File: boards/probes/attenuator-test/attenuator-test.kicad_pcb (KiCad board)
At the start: 4 copper layers, 45.6 x 10 mm, 7 parts, among them J1 Conn_Coaxial, J2 Conn_Coaxial

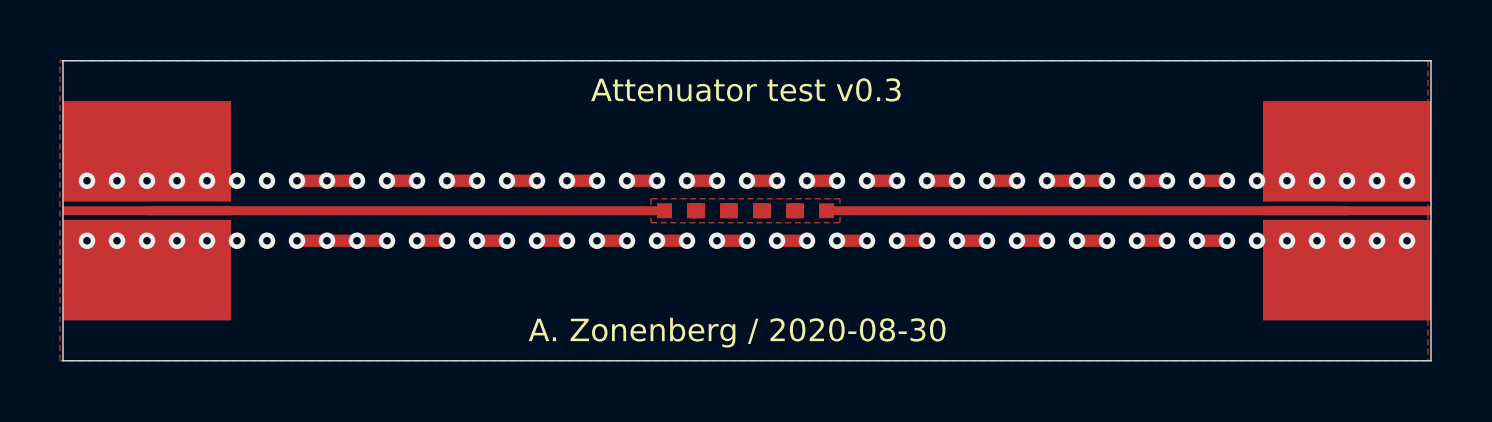
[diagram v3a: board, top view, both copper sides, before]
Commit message: Updated attenuator test with 4 overlapping resistor footprints
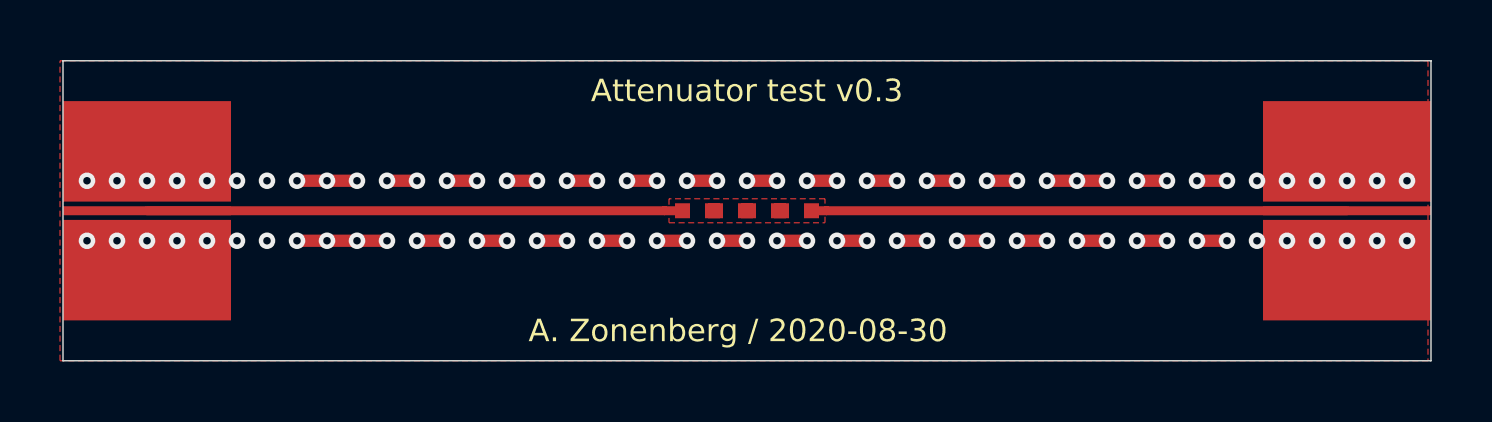
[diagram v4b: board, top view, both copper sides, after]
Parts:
- removed R2: 50, azonenberg_pcb:EIA_0402_RES_NOSILK_FLIPCHIP
- R3: value 100 -> 50
- R6: value 100 -> 200
- moved R3 0.50 mm to (128.3, 80.0)
- moved R4 0.50 mm to (129.4, 80.0)
- moved R5 0.50 mm to (130.6, 80.0)
- moved R6 0.50 mm to (131.7, 80.0)
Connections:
- R3 pad 2: Net-(R2-Pad1) -> /SIGNAL
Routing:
- net /SIGNAL: track 17.2 -> 17.8 mm
- net Net-(J2-Pad1): track 17.3 -> 17.8 mm
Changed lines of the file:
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@@
     (thickness 1.6)
     (drawings 6)
-    (tracks 184)
+    (tracks 186)
     (zones 0)
-    (modules 7)
-    (nets 8)
+    (modules 6)
+    (nets 7)
   )
   (page A4)
@@
   (net 2 /SIGNAL)
   (net 3 "Net-(J2-Pad1)")
-  (net 4 "Net-(R2-Pad1)")
-  (net 5 "Net-(R3-Pad1)")
-  (net 6 "Net-(R4-Pad1)")
-  (net 7 "Net-(R5-Pad1)")
+  (net 4 "Net-(R3-Pad1)")
+  (net 5 "Net-(R4-Pad1)")
+  (net 6 "Net-(R5-Pad1)")
   (net_class Default "This is the default net class."
     (clearance 0.15)
@@
     (add_net /SIGNAL)
     (add_net "Net-(J2-Pad1)")
-    (add_net "Net-(R2-Pad1)")
     (add_net "Net-(R3-Pad1)")
     (add_net "Net-(R4-Pad1)")
@@
   )
   (module azonenberg_pcb:EIA_0402_RES_NOSILK_FLIPCHIP (layer F.Cu)
-    (at 132.15 80 180)
+    (at 131.65 80 180)
     (solder_paste_margin -0.06)
     (fp_text reference R6 (at 0 1.5) (layer F.SilkS) hide
       (effects (font (size 1 1) (thickness 0.15)))
     )
-    (fp_text value 100 (at 0 3.5) (layer F.SilkS) hide
+    (fp_text value 200 (at 0 3.5) (layer F.SilkS) hide
       (effects (font (size 1 1) (thickness 0.15)))
     )
     (pad 2 smd rect (at 0.5 0 180) (size 0.5 0.5) (layers F.Cu F.Paste F.Mask)
-      (net 7 "Net-(R5-Pad1)"))
+      (net 6 "Net-(R5-Pad1)"))
     (pad 1 smd rect (at -0.5 0 180) (size 0.5 0.5) (layers F.Cu F.Paste F.Mask)
       (net 3 "Net-(J2-Pad1)"))
@@
   )
   (module azonenberg_pcb:EIA_0402_RES_NOSILK_FLIPCHIP (layer F.Cu)
-    (at 131.05 80 180)
+    (at 130.55 80 180)
     (solder_paste_margin -0.06)
     (fp_text reference R5 (at 0 1.5) (layer F.SilkS) hide
@@
     )
     (pad 2 smd rect (at 0.5 0 180) (size 0.5 0.5) (layers F.Cu F.Paste F.Mask)
-      (net 6 "Net-(R4-Pad1)"))
+      (net 5 "Net-(R4-Pad1)"))
     (pad 1 smd rect (at -0.5 0 180) (size 0.5 0.5) (layers F.Cu F.Paste F.Mask)
-      (net 7 "Net-(R5-Pad1)"))
+      (net 6 "Net-(R5-Pad1)"))
     (model /nfs4/home/azonenberg/kicad-libs/3rdparty/walter/smd_resistors/r_0402.wrl
       (at (xyz 0 0 0))
@@
   )
   (module azonenberg_pcb:EIA_0402_RES_NOSILK_FLIPCHIP (layer F.Cu)
-    (at 129.95 80 180)
+    (at 129.45 80 180)
     (solder_paste_margin -0.06)
     (fp_text reference R4 (at 0 1.5) (layer F.SilkS) hide
@@
     )
     (pad 2 smd rect (at 0.5 0 180) (size 0.5 0.5) (layers F.Cu F.Paste F.Mask)
-      (net 5 "Net-(R3-Pad1)"))
+      (net 4 "Net-(R3-Pad1)"))
     (pad 1 smd rect (at -0.5 0 180) (size 0.5 0.5) (layers F.Cu F.Paste F.Mask)
-      (net 6 "Net-(R4-Pad1)"))
+      (net 5 "Net-(R4-Pad1)"))
     (model /nfs4/home/azonenberg/kicad-libs/3rdparty/walter/smd_resistors/r_0402.wrl
       (at (xyz 0 0 0))
@@
   )
   (module azonenberg_pcb:EIA_0402_RES_NOSILK_FLIPCHIP (layer F.Cu)
-    (at 128.85 80 180)
+    (at 128.35 80 180)
     (solder_paste_margin -0.06)
     (fp_text reference R3 (at 0 1.5) (layer F.SilkS) hide
-      (effects (font (size 1 1) (thickness 0.15)))
-    )
-    (fp_text value 100 (at 0 3.5) (layer F.SilkS) hide
-      (effects (font (size 1 1) (thickness 0.15)))
-    )
-    (pad 2 smd rect (at 0.5 0 180) (size 0.5 0.5) (layers F.Cu F.Paste F.Mask)
-      (net 4 "Net-(R2-Pad1)"))
-    (pad 1 smd rect (at -0.5 0 180) (size 0.5 0.5) (layers F.Cu F.Paste F.Mask)
-      (net 5 "Net-(R3-Pad1)"))
-    (model /nfs4/home/azonenberg/kicad-libs/3rdparty/walter/smd_resistors/r_0402.wrl
-      (at (xyz 0 0 0))
-      (scale (xyz 1 1 1))
-      (rotate (xyz 0 0 0))
-    )
-  )
-  (module azonenberg_pcb:EIA_0402_RES_NOSILK_FLIPCHIP (layer F.Cu)
-    (at 127.75 80 180)
-    (solder_paste_margin -0.06)
-    (fp_text reference R2 (at 0 1.5) (layer F.SilkS) hide
       (effects (font (size 1 1) (thickness 0.15)))
     )
@@
       (net 2 /SIGNAL))
     (pad 1 smd rect (at -0.5 0 180) (size 0.5 0.5) (layers F.Cu F.Paste F.Mask)
-      (net 4 "Net-(R2-Pad1)"))
+      (net 4 "Net-(R3-Pad1)"))
     (model /nfs4/home/azonenberg/kicad-libs/3rdparty/walter/smd_resistors/r_0402.wrl
       (at (xyz 0 0 0))
@@
   (segment (start 151 81) (end 152 81) (width 0.3) (layer F.Cu) (net 1) (status 30))
   (segment (start 127.25 80) (end 110 80) (width 0.3) (layer F.Cu) (net 2) (status 30))
+  (segment (start 127.25 80) (end 127.85 80) (width 0.3) (layer F.Cu) (net 2))
   (segment (start 132.65 80) (end 150 80) (width 0.3) (layer F.Cu) (net 3) (status 30))
+  (segment (start 132.65 80) (end 132.15 80) (width 0.3) (layer F.Cu) (net 3))
   (zone (net 1) (net_name /GND) (layer In1.Cu) (hatch edge 0.508)
     (connect_pads yes (clearance 0.2))
@@
     (polygon
       (pts
-        (xy 126.8 79.6) (xy 126.8 80.4) (xy 133.1 80.4) (xy 133.1 79.6)
+        (xy 127.4 79.6) (xy 127.4 80.4) (xy 132.6 80.4) (xy 132.6 79.6)
       )
     )
@@
     (polygon
       (pts
-        (xy 126.5 79.5) (xy 126.5 80.5) (xy 126.7 80.5) (xy 126.7 79.5)
-      )
-    )
-    (polygon
-      (pts
-        (xy 133.2 79.5) (xy 133.2 80.5) (xy 133.4 80.5) (xy 133.4 79.5)
-      )
-    )
+        (xy 127.1 79.5) (xy 127.1 80.5) (xy 127.3 80.5) (xy 127.3 79.5)
+      )
+    )
+    (polygon
+      (pts
+        (xy 132.7 79.5) (xy 132.7 80.5) (xy 132.9 80.5) (xy 132.9 79.5)
+      )
+    )

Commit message: Attenuator test with 3 resistors
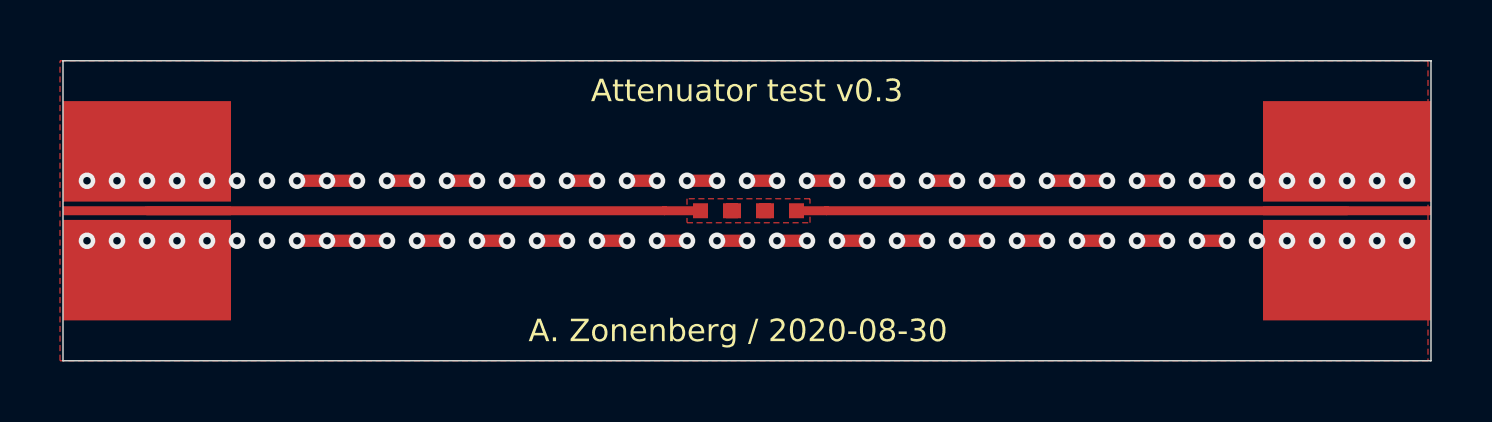
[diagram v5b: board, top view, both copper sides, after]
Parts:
- removed R3: 50, azonenberg_pcb:EIA_0402_RES_NOSILK_FLIPCHIP
- R4: value 100 -> 50
- R5: value 100 -> 200
- moved R4 0.50 mm to (128.9, 80.0)
- moved R5 0.50 mm to (130.1, 80.0)
- moved R6 0.50 mm to (131.2, 80.0)
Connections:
- R4 pad 2: Net-(R3-Pad1) -> /SIGNAL
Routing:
- net /SIGNAL: track 17.8 -> 18.4 mm
- net Net-(J2-Pad1): track 17.8 -> 18.3 mm
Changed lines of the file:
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@@
     (tracks 186)
     (zones 0)
-    (modules 6)
-    (nets 7)
+    (modules 5)
+    (nets 6)
   )
   (page A4)
@@
   (net 2 /SIGNAL)
   (net 3 "Net-(J2-Pad1)")
-  (net 4 "Net-(R3-Pad1)")
-  (net 5 "Net-(R4-Pad1)")
-  (net 6 "Net-(R5-Pad1)")
+  (net 4 "Net-(R4-Pad1)")
+  (net 5 "Net-(R5-Pad1)")
   (net_class Default "This is the default net class."
     (clearance 0.15)
@@
     (add_net /SIGNAL)
     (add_net "Net-(J2-Pad1)")
-    (add_net "Net-(R3-Pad1)")
     (add_net "Net-(R4-Pad1)")
     (add_net "Net-(R5-Pad1)")
   )
   (module azonenberg_pcb:EIA_0402_RES_NOSILK_FLIPCHIP (layer F.Cu)
-    (at 131.65 80 180)
+    (at 131.15 80 180)
     (solder_paste_margin -0.06)
     (fp_text reference R6 (at 0 1.5) (layer F.SilkS) hide
@@
     )
     (pad 2 smd rect (at 0.5 0 180) (size 0.5 0.5) (layers F.Cu F.Paste F.Mask)
-      (net 6 "Net-(R5-Pad1)"))
+      (net 5 "Net-(R5-Pad1)"))
     (pad 1 smd rect (at -0.5 0 180) (size 0.5 0.5) (layers F.Cu F.Paste F.Mask)
       (net 3 "Net-(J2-Pad1)"))
@@
   )
   (module azonenberg_pcb:EIA_0402_RES_NOSILK_FLIPCHIP (layer F.Cu)
-    (at 130.55 80 180)
+    (at 130.05 80 180)
     (solder_paste_margin -0.06)
     (fp_text reference R5 (at 0 1.5) (layer F.SilkS) hide
       (effects (font (size 1 1) (thickness 0.15)))
     )
-    (fp_text value 100 (at 0 3.5) (layer F.SilkS) hide
+    (fp_text value 200 (at 0 3.5) (layer F.SilkS) hide
       (effects (font (size 1 1) (thickness 0.15)))
     )
     (pad 2 smd rect (at 0.5 0 180) (size 0.5 0.5) (layers F.Cu F.Paste F.Mask)
-      (net 5 "Net-(R4-Pad1)"))
+      (net 4 "Net-(R4-Pad1)"))
     (pad 1 smd rect (at -0.5 0 180) (size 0.5 0.5) (layers F.Cu F.Paste F.Mask)
-      (net 6 "Net-(R5-Pad1)"))
+      (net 5 "Net-(R5-Pad1)"))
     (model /nfs4/home/azonenberg/kicad-libs/3rdparty/walter/smd_resistors/r_0402.wrl
       (at (xyz 0 0 0))
@@
   )
   (module azonenberg_pcb:EIA_0402_RES_NOSILK_FLIPCHIP (layer F.Cu)
-    (at 129.45 80 180)
+    (at 128.95 80 180)
     (solder_paste_margin -0.06)
     (fp_text reference R4 (at 0 1.5) (layer F.SilkS) hide
-      (effects (font (size 1 1) (thickness 0.15)))
-    )
-    (fp_text value 100 (at 0 3.5) (layer F.SilkS) hide
-      (effects (font (size 1 1) (thickness 0.15)))
-    )
-    (pad 2 smd rect (at 0.5 0 180) (size 0.5 0.5) (layers F.Cu F.Paste F.Mask)
-      (net 4 "Net-(R3-Pad1)"))
-    (pad 1 smd rect (at -0.5 0 180) (size 0.5 0.5) (layers F.Cu F.Paste F.Mask)
-      (net 5 "Net-(R4-Pad1)"))
-    (model /nfs4/home/azonenberg/kicad-libs/3rdparty/walter/smd_resistors/r_0402.wrl
-      (at (xyz 0 0 0))
-      (scale (xyz 1 1 1))
-      (rotate (xyz 0 0 0))
-    )
-  )
-  (module azonenberg_pcb:EIA_0402_RES_NOSILK_FLIPCHIP (layer F.Cu)
-    (at 128.35 80 180)
-    (solder_paste_margin -0.06)
-    (fp_text reference R3 (at 0 1.5) (layer F.SilkS) hide
       (effects (font (size 1 1) (thickness 0.15)))
     )
@@
       (net 2 /SIGNAL))
     (pad 1 smd rect (at -0.5 0 180) (size 0.5 0.5) (layers F.Cu F.Paste F.Mask)
-      (net 4 "Net-(R3-Pad1)"))
+      (net 4 "Net-(R4-Pad1)"))
     (model /nfs4/home/azonenberg/kicad-libs/3rdparty/walter/smd_resistors/r_0402.wrl
       (at (xyz 0 0 0))
@@
   (via (at 152 81) (size 0.55) (drill 0.25) (layers F.Cu B.Cu) (net 1) (status 30))
   (segment (start 151 81) (end 152 81) (width 0.3) (layer F.Cu) (net 1) (status 30))
-  (segment (start 127.25 80) (end 110 80) (width 0.3) (layer F.Cu) (net 2) (status 30))
-  (segment (start 127.25 80) (end 127.85 80) (width 0.3) (layer F.Cu) (net 2))
-  (segment (start 132.65 80) (end 150 80) (width 0.3) (layer F.Cu) (net 3) (status 30))
-  (segment (start 132.65 80) (end 132.15 80) (width 0.3) (layer F.Cu) (net 3))
+  (segment (start 127.25 80) (end 110 80) (width 0.3) (layer F.Cu) (net 2))
+  (segment (start 128.45 80) (end 127.25 80) (width 0.3) (layer F.Cu) (net 2))
+  (segment (start 132.65 80) (end 150 80) (width 0.3) (layer F.Cu) (net 3))
+  (segment (start 131.65 80) (end 132.65 80) (width 0.3) (layer F.Cu) (net 3))
   (zone (net 1) (net_name /GND) (layer In1.Cu) (hatch edge 0.508)
     (connect_pads yes (clearance 0.2))
@@
     (polygon
       (pts
-        (xy 127.4 79.6) (xy 127.4 80.4) (xy 132.6 80.4) (xy 132.6 79.6)
+        (xy 128 79.6) (xy 128 80.4) (xy 132.1 80.4) (xy 132.1 79.6)
       )
     )
@@
     (polygon
       (pts
-        (xy 127.1 79.5) (xy 127.1 80.5) (xy 127.3 80.5) (xy 127.3 79.5)
-      )
-    )
-    (polygon
-      (pts
-        (xy 132.7 79.5) (xy 132.7 80.5) (xy 132.9 80.5) (xy 132.9 79.5)
-      )
-    )
+        (xy 127.7 79.5) (xy 127.7 80.5) (xy 127.9 80.5) (xy 127.9 79.5)
+      )
+    )
+    (polygon
+      (pts
+        (xy 132.2 79.5) (xy 132.2 80.5) (xy 132.4 80.5) (xy 132.4 79.5)
+      )
+    )
